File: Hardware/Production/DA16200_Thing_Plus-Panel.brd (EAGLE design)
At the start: 200.2 x 144.3 mm, 2086 parts, among them J1 Qwiic, J10 CORTEX_JTAG_DEBUG_PTH_NS, J11 Qwiic, J13 USB C, J14 THING_PLUS, J15 CORTEX_JTAG_DEBUG_PTH_NS, J16 Qwiic, J18 USB C, J19 THING_PLUS, J2 THING_PLUS, J20 CORTEX_JTAG_DEBUG_PTH_NS, J21 Qwiic, J23 USB C, J24 THING_PLUS, J25 CORTEX_JTAG_DEBUG_PTH_NS, J26 Qwiic, J28 USB C, J29 THING_PLUS, J3 Qwiic, J30 CORTEX_JTAG_DEBUG_PTH_NS, J31 Qwiic, J33 USB C, J34 THING_PLUS, J35 CORTEX_JTAG_DEBUG_PTH_NS, J36 Qwiic, J38 USB C, J39 THING_PLUS, J40 CORTEX_JTAG_DEBUG_PTH_NS, J41 Qwiic, J43 USB C, J44 THING_PLUS, J45 CORTEX_JTAG_DEBUG_PTH_NS, J46 Qwiic, J48 USB C, J49 THING_PLUS, J5 USB C, J50 CORTEX_JTAG_DEBUG_PTH_NS, J51 Qwiic, J53 USB C, J54 THING_PLUS, J55 CORTEX_JTAG_DEBUG_PTH_NS, J56 Qwiic, J58 USB C, J59 THING_PLUS, J60 CORTEX_JTAG_DEBUG_PTH_NS, J61 Qwiic, J63 USB C, J64 THING_PLUS, J65 CORTEX_JTAG_DEBUG_PTH_NS, J66 Qwiic, J68 USB C, J69 THING_PLUS, J7 CORTEX_JTAG_DEBUG_PTH_NS, J70 CORTEX_JTAG_DEBUG_PTH_NS, J71 Qwiic, J73 USB C, J74 THING_PLUS, J75 CORTEX_JTAG_DEBUG_PTH_NS, J76 Qwiic, J78 USB C, J79 THING_PLUS, J8 USB C, J80 CORTEX_JTAG_DEBUG_PTH_NS, J9 THING_PLUS, Q1 20V/4.2A/52mΩ/1.4W, Q10 20V/4.2A/52mΩ/1.4W, Q11 20V/4.2A/52mΩ/1.4W, Q12 20V/4.2A/52mΩ/1.4W, Q13 20V/4.2A/52mΩ/1.4W, Q14 20V/4.2A/52mΩ/1.4W, Q15 20V/4.2A/52mΩ/1.4W, Q16 20V/4.2A/52mΩ/1.4W, Q2 20V/4.2A/52mΩ/1.4W, Q3 20V/4.2A/52mΩ/1.4W, Q4 20V/4.2A/52mΩ/1.4W, Q5 20V/4.2A/52mΩ/1.4W, Q6 20V/4.2A/52mΩ/1.4W, Q7 20V/4.2A/52mΩ/1.4W, Q8 20V/4.2A/52mΩ/1.4W, Q9 20V/4.2A/52mΩ/1.4W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

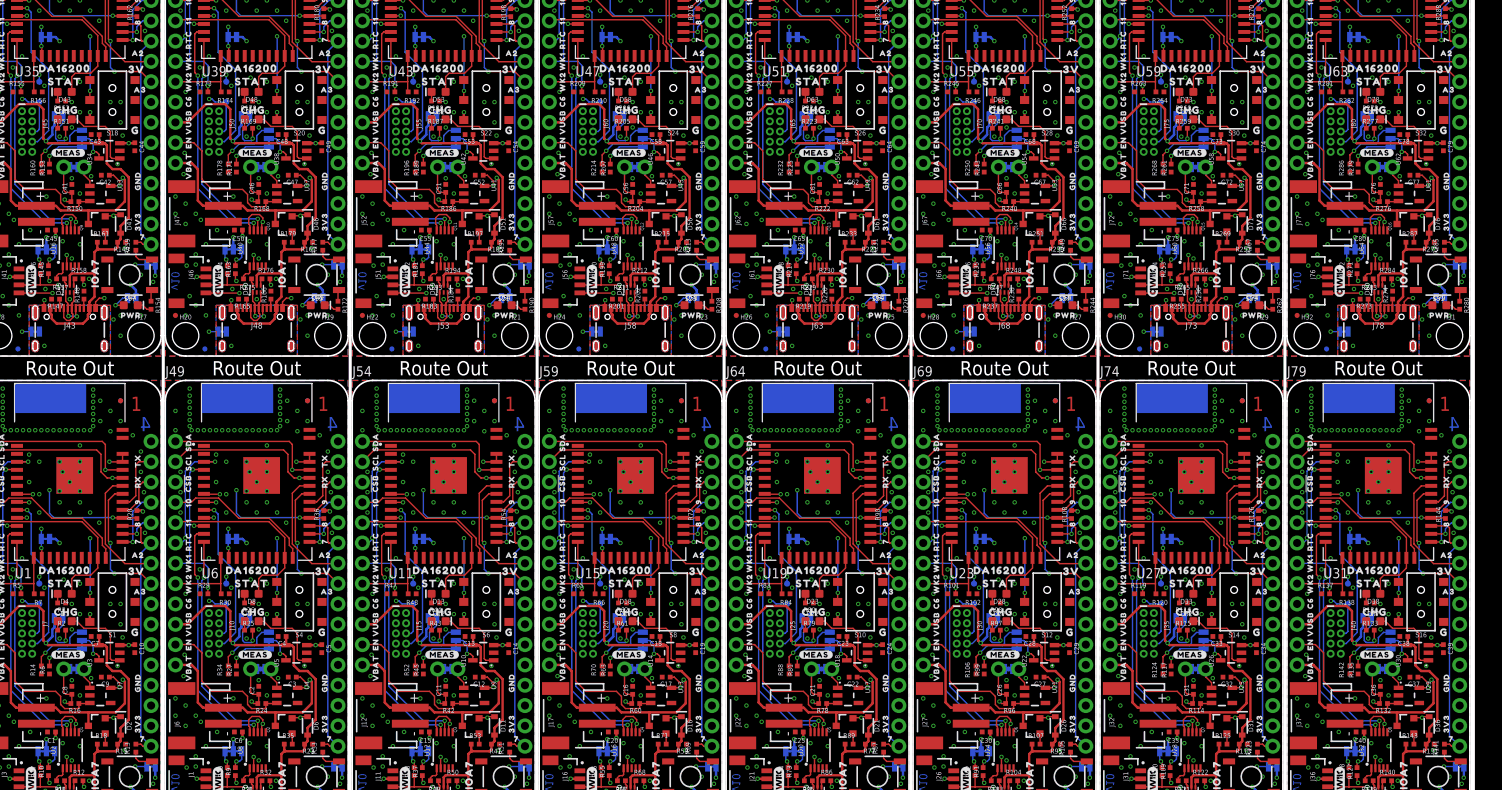
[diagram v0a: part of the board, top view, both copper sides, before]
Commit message: re-panelize
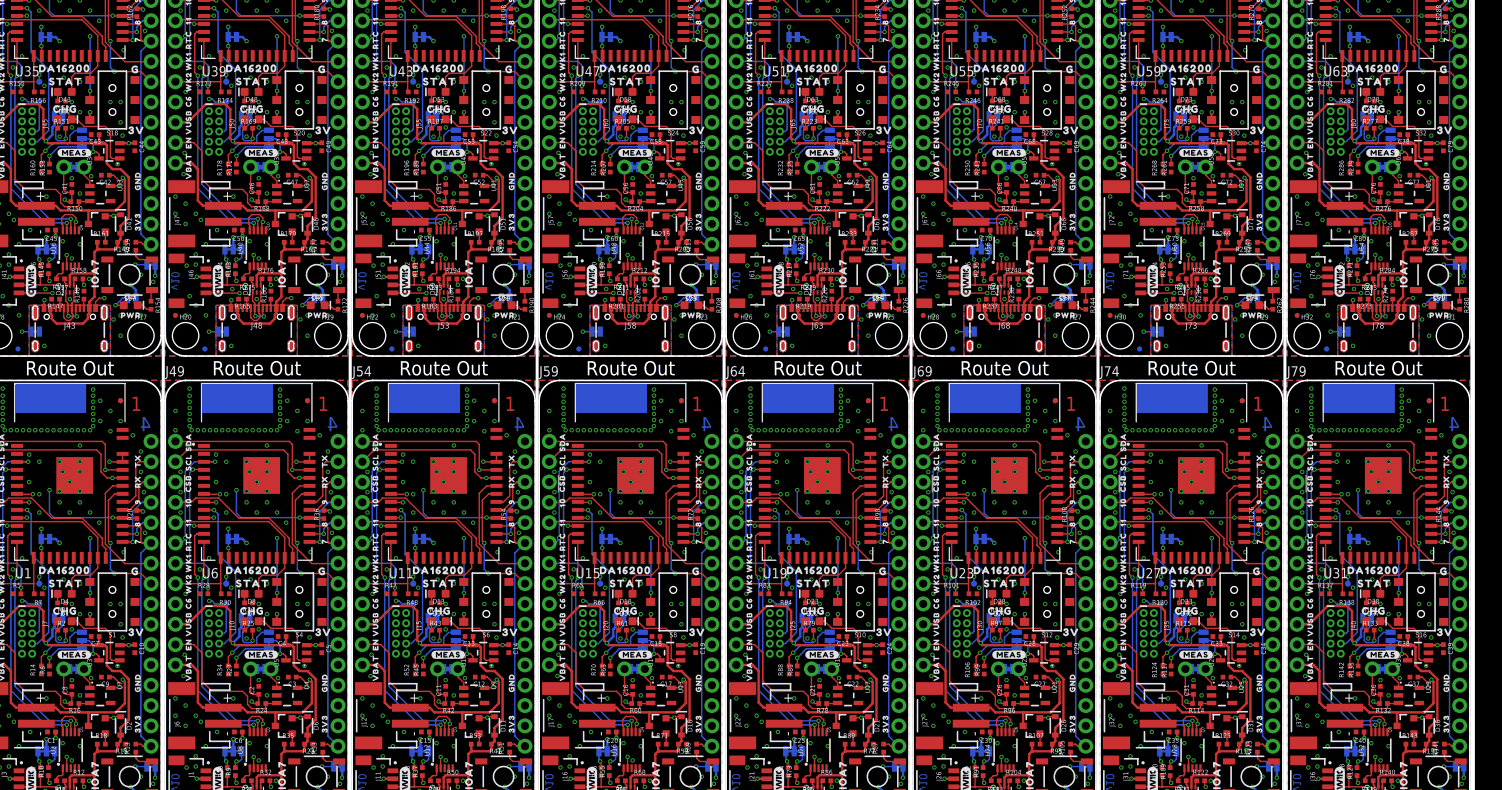
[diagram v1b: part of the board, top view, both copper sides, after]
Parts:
- removed U$1105, U$1106, U$1107, U$1108, U$1109, U$1124: (no value), output:#NC#0
- removed U$1110: (no value), output:5000
- removed U$1111: (no value), output:1000
- removed U$1112: (no value), output:MA0
- removed U$1113: (no value), output:SDA0
- removed U$1114: (no value), output:SCL0
- removed U$1115: (no value), output:#CSB#0
- removed U$1116: (no value), output:100
- removed U$1117: (no value), output:RTC0
- removed U$1118: (no value), output:WK10
- removed U$1119: (no value), output:WK20
- removed U$1120: (no value), output:EN0
- removed U$1121: (no value), output:VUSB0
- removed U$1122: (no value), output:VBAT0
- removed U$1123: (no value), output:110
- removed U$1125: (no value), output:TX0
- removed U$1126: (no value), output:RX0
- removed U$1127: (no value), output:90
- removed U$1128: (no value), output:80
- removed U$1129, U$1134: (no value), output:70
- removed U$1130: (no value), output:A20
- removed U$1131: (no value), output:A30
- removed U$1132: (no value), output:GND0
- removed U$1133: (no value), output:3V30
- removed U$1135: (no value), output:#CHG#0
- removed U$1136: (no value), output:#CH340#0
- removed U$1137: (no value), output:#0#SDA#0
- removed U$1138: (no value), output:#1#SCL#0
- removed U$1139: (no value), output:#6##CSB##0
- removed U$1140: (no value), output:#11#LED#0
- removed U$1141: (no value), output:C60
- removed U$1142: (no value), output:#IOA10#0
- removed U$1143: (no value), output:#4#TXO#0
- removed U$1144: (no value), output:#5#RXI#0
- removed U$1145: (no value), output:#9#POCI#0
- removed U$1146: (no value), output:#8#PICO#0
- removed U$1147: (no value), output:#7#SCLK#0
- removed U$1148: (no value), output:#2#A2#0
- removed U$1149: (no value), output:#3#A3#0
- removed U$1150: (no value), output:#DA#0
- removed U$1151: (no value), output:#MEAS#0
- removed U$1152: (no value), output:#VBAT#0
- U$100, U$169: device output:#NC#0 -> output:1000
- U$1000: device output:#5#RXI#0 -> output:SCL0
- U$1001: device output:#9#POCI#0 -> output:#CSB#0
- U$1002: device output:#8#PICO#0 -> output:100
- U$1003: device output:#7#SCLK#0 -> output:RTC0
- U$1004: device output:#2#A2#0 -> output:WK10
- U$1005: device output:#3#A3#0 -> output:WK20
- U$1006: device output:#DA#0 -> output:EN0
- U$1007: device output:#MEAS#0 -> output:VUSB0
- U$1008: device output:#VBAT#0 -> output:VBAT0
- U$1009: device SparkFun-Aesthetics:QWIIC_4MM -> output:110
- U$101, U$170: device output:#NC#0 -> output:MA0
- U$1010, U$578, U$650: device output:PWR0 -> output:#NC#0
- U$1011: device output:#GND#0 -> output:TX0
- U$1012: device output:#3V3#0 -> output:RX0
- U$1013: device output:#EN#0 -> output:90
- U$1014: device output:#IOC6#0 -> output:80
- U$1015: device output:#WK2#0 -> output:70
- U$1016: device output:#WK1#0 -> output:GND0
- U$1017: device output:#RTC#0 -> output:3V30
- U$1018: device output:THING_PLUS0 -> output:#CHG#0
- U$1019: device output:DA162000 -> output:#CH340#0
- U$102: device output:5000 -> output:SDA0
- U$1020: device output:DA162000 -> output:#0#SDA#0
- U$1021: device output:#I�C#0 -> output:#1#SCL#0
- U$1022: device output:#LED#0 -> output:#6##CSB##0
- U$1023: device output:#SHLD#0 -> output:#11#LED#0
- U$1024: device output:STAT0 -> output:C60
- U$1025: device output:CHG0 -> output:#IOA10#0
- U$1026: device output:##RST##0 -> output:#4#TXO#0
- U$1027: device output:#MEAS#0 -> output:#5#RXI#0
- U$1028: device output:#MEAS_#0 -> output:#9#POCI#0
- U$1029: device output:G0 -> output:#8#PICO#0
- U$103: device output:1000 -> output:SCL0
- U$1030: device output:3V0 -> output:#7#SCLK#0
- U$1031: device output:IOA7_0 -> output:#2#A2#0
- U$1032: device output:#VU#0 -> output:#3#A3#0
- U$1033, U$964: device output:#NC#0 -> output:#DA#0
- U$1034, U$620, U$965: device output:#NC#0 -> output:#MEAS#0
- U$1035: device output:#NC#0 -> output:#VBAT#0
- U$1036: device output:#NC#0 -> SparkFun-Aesthetics:QWIIC_4MM
- U$1037, U$692: device output:#NC#0 -> output:PWR0
- U$1038: device output:5000 -> output:#GND#0
- U$1039: device output:1000 -> output:#3V3#0
- U$104: device output:MA0 -> output:#CSB#0
- U$1040: device output:MA0 -> output:#EN#0
- U$1041: device output:SDA0 -> output:#IOC6#0
- U$1042: device output:SCL0 -> output:#WK2#0
- U$1043: device output:#CSB#0 -> output:#WK1#0
- U$1044: device output:100 -> output:#RTC#0
- U$1045: device output:RTC0 -> output:THING_PLUS0
- U$1046: device output:WK10 -> output:DA162000
- U$1047: device output:WK20 -> output:DA162000
- U$1048: device output:EN0 -> output:#I�C#0
- U$1049: device output:VUSB0 -> output:#LED#0
- U$105: device output:SDA0 -> output:100
- U$1050: device output:VBAT0 -> output:#SHLD#0
- U$1051: device output:110 -> output:STAT0
- U$1052: device output:#NC#0 -> output:CHG0
- U$1053: device output:TX0 -> output:##RST##0
- U$1054: device output:RX0 -> output:#MEAS#0
- U$1055: device output:90 -> output:#MEAS_#0
- U$1056: device output:80 -> output:G0
- U$1057: device output:70 -> output:3V0
- U$1058: device output:A20 -> output:IOA7_0
- U$1059: device output:A30 -> output:#VU#0
- U$106: device output:SCL0 -> output:RTC0
- U$1060: device output:GND0 -> output:#NC#0
- U$1061: device output:3V30 -> output:#NC#0
- U$1062: device output:70 -> output:#NC#0
- U$1063, U$991: device output:#CHG#0 -> output:#NC#0
- U$1064, U$992: device output:#CH340#0 -> output:#NC#0
- U$1065: device output:#0#SDA#0 -> output:5000
- U$1066: device output:#1#SCL#0 -> output:1000
- U$1067: device output:#6##CSB##0 -> output:MA0
- U$1068: device output:#11#LED#0 -> output:SDA0
- U$1069: device output:C60 -> output:SCL0
- U$107: device output:#CSB#0 -> output:WK10
- U$1070: device output:#IOA10#0 -> output:#CSB#0
- U$1071: device output:#4#TXO#0 -> output:100
- U$1072: device output:#5#RXI#0 -> output:RTC0
- U$1073: device output:#9#POCI#0 -> output:WK10
- U$1074: device output:#8#PICO#0 -> output:WK20
- U$1075: device output:#7#SCLK#0 -> output:EN0
- U$1076: device output:#2#A2#0 -> output:VUSB0
- U$1077: device output:#3#A3#0 -> output:VBAT0
- U$1078: device output:#DA#0 -> output:110
- U$1079, U$163, U$235, U$647, U$719: device output:#MEAS#0 -> output:#NC#0
- U$108: device output:100 -> output:WK20
- U$1080: device output:#VBAT#0 -> output:TX0
- U$1081: device SparkFun-Aesthetics:QWIIC_4MM -> output:RX0
- U$1082: device output:PWR0 -> output:90
- U$1083: device output:#GND#0 -> output:80
- U$1084: device output:#3V3#0 -> output:70
- U$1085: device output:#EN#0 -> output:GND0
- U$1086: device output:#IOC6#0 -> output:3V30
- U$1087: device output:#WK2#0 -> output:#CHG#0
- U$1088: device output:#WK1#0 -> output:#CH340#0
- U$1089: device output:#RTC#0 -> output:#0#SDA#0
- U$109: device output:RTC0 -> output:EN0
- U$1090: device output:THING_PLUS0 -> output:#1#SCL#0
- U$1091: device output:DA162000 -> output:#6##CSB##0
- U$1092: device output:DA162000 -> output:#11#LED#0
- U$1093: device output:#I�C#0 -> output:C60
- U$1094: device output:#LED#0 -> output:#IOA10#0
- U$1095: device output:#SHLD#0 -> output:#4#TXO#0
- U$1096: device output:STAT0 -> output:#5#RXI#0
- U$1097: device output:CHG0 -> output:#9#POCI#0
- U$1098: device output:##RST##0 -> output:#8#PICO#0
- U$1099: device output:#MEAS#0 -> output:#7#SCLK#0
- U$110: device output:WK10 -> output:VUSB0
- U$1100: device output:#MEAS_#0 -> output:#2#A2#0
- U$1101: device output:G0 -> output:#3#A3#0
- U$1102: device output:3V0 -> output:#DA#0
- U$1103: device output:IOA7_0 -> output:#MEAS#0
- U$1104: device output:#VU#0 -> output:#VBAT#0
- U$111: device output:WK20 -> output:VBAT0
- U$112: device output:EN0 -> output:110
- U$113: device output:VUSB0 -> output:#NC#0
- U$114: device output:VBAT0 -> output:TX0
- U$115: device output:110 -> output:RX0
- U$116, U$461, U$530: device output:#NC#0 -> output:90
- U$117: device output:TX0 -> output:80
- U$118: device output:RX0 -> output:70
- U$119: device output:90 -> output:GND0
- U$120: device output:80 -> output:3V30
- U$121: device output:70 -> output:#CHG#0
- U$122: device output:A20 -> output:#CH340#0
- U$123: device output:A30 -> output:#0#SDA#0
- U$124: device output:GND0 -> output:#1#SCL#0
- U$125: device output:3V30 -> output:#6##CSB##0
- U$126: device output:70 -> output:#11#LED#0
- U$127: device output:#CHG#0 -> output:C60
- U$128: device output:#CH340#0 -> output:#IOA10#0
- U$129: device output:#0#SDA#0 -> output:#4#TXO#0
- U$130: device output:#1#SCL#0 -> output:#5#RXI#0
- U$131: device output:#6##CSB##0 -> output:#9#POCI#0
- U$132: device output:#11#LED#0 -> output:#8#PICO#0
- U$133: device output:C60 -> output:#7#SCLK#0
- U$134: device output:#IOA10#0 -> output:#2#A2#0
- U$135: device output:#4#TXO#0 -> output:#3#A3#0
- U$136: device output:#5#RXI#0 -> output:#DA#0
- U$137: device output:#9#POCI#0 -> output:#MEAS#0
- U$138: device output:#8#PICO#0 -> output:#VBAT#0
- U$139: device output:#7#SCLK#0 -> SparkFun-Aesthetics:QWIIC_4MM
- U$140: device output:#2#A2#0 -> output:PWR0
- U$141: device output:#3#A3#0 -> output:#GND#0
- U$142: device output:#DA#0 -> output:#3V3#0
- U$143: device output:#MEAS#0 -> output:#EN#0
- U$144: device output:#VBAT#0 -> output:#IOC6#0
- U$145: device SparkFun-Aesthetics:QWIIC_4MM -> output:#WK2#0
- U$146: device output:PWR0 -> output:#WK1#0
- U$147: device output:#GND#0 -> output:#RTC#0
- U$148: device output:#3V3#0 -> output:THING_PLUS0
- U$149: device output:#EN#0 -> output:DA162000
- U$150: device output:#IOC6#0 -> output:DA162000
- U$151: device output:#WK2#0 -> output:#I�C#0
- U$152: device output:#WK1#0 -> output:#LED#0
- U$153: device output:#RTC#0 -> output:#SHLD#0
- U$154: device output:THING_PLUS0 -> output:STAT0
- U$155: device output:DA162000 -> output:CHG0
- U$156: device output:DA162000 -> output:##RST##0
- U$157: device output:#I�C#0 -> output:#MEAS#0
- U$158: device output:#LED#0 -> output:#MEAS_#0
- U$159: device output:#SHLD#0 -> output:G0
- U$160: device output:STAT0 -> output:3V0
- U$161: device output:CHG0 -> output:IOA7_0
- U$162: device output:##RST##0 -> output:#VU#0
- U$164, U$236, U$596: device output:#MEAS_#0 -> output:#NC#0
- U$165: device output:G0 -> output:#NC#0
- U$166, U$94: device output:3V0 -> output:#NC#0
- U$167, U$527, U$95: device output:IOA7_0 -> output:#NC#0
- U$168: device output:#VU#0 -> output:5000
- U$171: device output:#NC#0 -> output:SDA0
- U$172, U$241: device output:#NC#0 -> output:SCL0
- U$173, U$242: device output:#NC#0 -> output:#CSB#0
- U$174: device output:5000 -> output:100
- U$175: device output:1000 -> output:RTC0
- U$176: device output:MA0 -> output:WK10
- U$177: device output:SDA0 -> output:WK20
- U$178: device output:SCL0 -> output:EN0
- U$179: device output:#CSB#0 -> output:VUSB0
- U$180: device output:100 -> output:VBAT0
- U$181: device output:RTC0 -> output:110
- U$182: device output:WK10 -> output:#NC#0
- U$183: device output:WK20 -> output:TX0
- U$184: device output:EN0 -> output:RX0
- U$185: device output:VUSB0 -> output:90
- U$186: device output:VBAT0 -> output:80
- U$187: device output:110 -> output:70
- U$188, U$533, U$602: device output:#NC#0 -> output:GND0
- U$189: device output:TX0 -> output:3V30
- U$190: device output:RX0 -> output:#CHG#0
- U$191: device output:90 -> output:#CH340#0
- U$192: device output:80 -> output:#0#SDA#0
- U$193: device output:70 -> output:#1#SCL#0
- U$194: device output:A20 -> output:#6##CSB##0
- U$195: device output:A30 -> output:#11#LED#0
- U$196: device output:GND0 -> output:C60
- U$197: device output:3V30 -> output:#IOA10#0
- U$198: device output:70 -> output:#4#TXO#0
- U$199: device output:#CHG#0 -> output:#5#RXI#0
- U$200: device output:#CH340#0 -> output:#9#POCI#0
- U$201: device output:#0#SDA#0 -> output:#8#PICO#0
- U$202: device output:#1#SCL#0 -> output:#7#SCLK#0
- U$203: device output:#6##CSB##0 -> output:#2#A2#0
- U$204: device output:#11#LED#0 -> output:#3#A3#0
- U$205: device output:C60 -> output:#DA#0
- U$206: device output:#IOA10#0 -> output:#MEAS#0
- U$207: device output:#4#TXO#0 -> output:#VBAT#0
- U$208: device output:#5#RXI#0 -> SparkFun-Aesthetics:QWIIC_4MM
- U$209: device output:#9#POCI#0 -> output:PWR0
- U$210: device output:#8#PICO#0 -> output:#GND#0
- U$211: device output:#7#SCLK#0 -> output:#3V3#0
- U$212: device output:#2#A2#0 -> output:#EN#0
- U$213: device output:#3#A3#0 -> output:#IOC6#0
- U$214: device output:#DA#0 -> output:#WK2#0
- U$215: device output:#MEAS#0 -> output:#WK1#0
- U$216: device output:#VBAT#0 -> output:#RTC#0
- U$217: device SparkFun-Aesthetics:QWIIC_4MM -> output:THING_PLUS0
- U$218: device output:PWR0 -> output:DA162000
- U$219: device output:#GND#0 -> output:DA162000
- U$220: device output:#3V3#0 -> output:#I�C#0
- U$221: device output:#EN#0 -> output:#LED#0
- U$222: device output:#IOC6#0 -> output:#SHLD#0
- U$223: device output:#WK2#0 -> output:STAT0
- U$224: device output:#WK1#0 -> output:CHG0
- U$225: device output:#RTC#0 -> output:##RST##0
- U$226: device output:THING_PLUS0 -> output:#MEAS#0
- U$227: device output:DA162000 -> output:#MEAS_#0
- U$228: device output:DA162000 -> output:G0
- U$229: device output:#I�C#0 -> output:3V0
- U$230: device output:#LED#0 -> output:IOA7_0
- U$231: device output:#SHLD#0 -> output:#VU#0
- U$232, U$304: device output:STAT0 -> output:#NC#0
- U$233, U$305, U$665: device output:CHG0 -> output:#NC#0
- U$234: device output:##RST##0 -> output:#NC#0
- U$237: device output:G0 -> output:5000
- U$238: device output:3V0 -> output:1000
- U$239: device output:IOA7_0 -> output:MA0
- U$240: device output:#VU#0 -> output:SDA0
- U$243: device output:#NC#0 -> output:100
- U$244, U$313: device output:#NC#0 -> output:RTC0
- U$245, U$314: device output:#NC#0 -> output:WK10
- U$246: device output:5000 -> output:WK20
- U$247: device output:1000 -> output:EN0
- U$248: device output:MA0 -> output:VUSB0
- U$249: device output:SDA0 -> output:VBAT0
- U$250: device output:SCL0 -> output:110
- U$251: device output:#CSB#0 -> output:#NC#0
- U$252: device output:100 -> output:TX0
- U$253: device output:RTC0 -> output:RX0
- U$254: device output:WK10 -> output:90
- U$255: device output:WK20 -> output:80
- U$256: device output:EN0 -> output:70
- U$257: device output:VUSB0 -> output:GND0
- U$258: device output:VBAT0 -> output:3V30
- U$259: device output:110 -> output:#CHG#0
- U$260, U$605, U$674: device output:#NC#0 -> output:#CH340#0
- U$261: device output:TX0 -> output:#0#SDA#0
- U$262: device output:RX0 -> output:#1#SCL#0
- U$263: device output:90 -> output:#6##CSB##0
- U$264: device output:80 -> output:#11#LED#0
- U$265: device output:70 -> output:C60
- U$266: device output:A20 -> output:#IOA10#0
- U$267: device output:A30 -> output:#4#TXO#0
- U$268: device output:GND0 -> output:#5#RXI#0
- U$269: device output:3V30 -> output:#9#POCI#0
- U$270: device output:70 -> output:#8#PICO#0
- U$271: device output:#CHG#0 -> output:#7#SCLK#0
- U$272: device output:#CH340#0 -> output:#2#A2#0
- U$273: device output:#0#SDA#0 -> output:#3#A3#0
- U$274: device output:#1#SCL#0 -> output:#DA#0
- U$275: device output:#6##CSB##0 -> output:#MEAS#0
- U$276: device output:#11#LED#0 -> output:#VBAT#0
- U$277: device output:C60 -> SparkFun-Aesthetics:QWIIC_4MM
- U$278: device output:#IOA10#0 -> output:PWR0
- U$279: device output:#4#TXO#0 -> output:#GND#0
- U$280: device output:#5#RXI#0 -> output:#3V3#0
- U$281: device output:#9#POCI#0 -> output:#EN#0
- U$282: device output:#8#PICO#0 -> output:#IOC6#0
- U$283: device output:#7#SCLK#0 -> output:#WK2#0
- U$284: device output:#2#A2#0 -> output:#WK1#0
- U$285: device output:#3#A3#0 -> output:#RTC#0
- U$286: device output:#DA#0 -> output:THING_PLUS0
- U$287: device output:#MEAS#0 -> output:DA162000
- U$288: device output:#VBAT#0 -> output:DA162000
- U$289: device SparkFun-Aesthetics:QWIIC_4MM -> output:#I�C#0
- U$290: device output:PWR0 -> output:#LED#0
- U$291: device output:#GND#0 -> output:#SHLD#0
- U$292: device output:#3V3#0 -> output:STAT0
- U$293: device output:#EN#0 -> output:CHG0
- U$294: device output:#IOC6#0 -> output:##RST##0
- U$295: device output:#WK2#0 -> output:#MEAS#0
- U$296: device output:#WK1#0 -> output:#MEAS_#0
- U$297: device output:#RTC#0 -> output:G0
- U$298: device output:THING_PLUS0 -> output:3V0
- U$299: device output:DA162000 -> output:IOA7_0
- U$300: device output:DA162000 -> output:#VU#0
- U$301, U$373: device output:#I�C#0 -> output:#NC#0
- U$302, U$374, U$734: device output:#LED#0 -> output:#NC#0
- U$303: device output:#SHLD#0 -> output:#NC#0
- U$306: device output:##RST##0 -> output:5000
- U$307: device output:#MEAS#0 -> output:1000
- U$308: device output:#MEAS_#0 -> output:MA0
- U$309: device output:G0 -> output:SDA0
- U$310: device output:3V0 -> output:SCL0
- U$311: device output:IOA7_0 -> output:#CSB#0
- U$312: device output:#VU#0 -> output:100
- U$315: device output:#NC#0 -> output:WK20
- U$316, U$385: device output:#NC#0 -> output:EN0
- U$317, U$386: device output:#NC#0 -> output:VUSB0
- U$318: device output:5000 -> output:VBAT0
- U$319: device output:1000 -> output:110
- U$320: device output:MA0 -> output:#NC#0
- U$321: device output:SDA0 -> output:TX0
- U$322: device output:SCL0 -> output:RX0
- U$323: device output:#CSB#0 -> output:90
- U$324: device output:100 -> output:80
- U$325: device output:RTC0 -> output:70
- U$326: device output:WK10 -> output:GND0
- U$327: device output:WK20 -> output:3V30
- U$328: device output:EN0 -> output:#CHG#0
- U$329: device output:VUSB0 -> output:#CH340#0
- U$330: device output:VBAT0 -> output:#0#SDA#0
- U$331: device output:110 -> output:#1#SCL#0
- U$332, U$677, U$746: device output:#NC#0 -> output:#6##CSB##0
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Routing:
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
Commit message: Final panel
Kasey generated and approved!
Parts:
- removed C61, C66, C71, C76: 1.0uF, SparkFun-Capacitors:0402-TIGHT
- removed C62, C67, C72, C77: 2.2uF, SparkFun-Capacitors:0402-TIGHT
- removed C63, C64, C68, C69, C73, C74, C78, C79: 4.7uF, SparkFun-Capacitors:0402-TIGHT
- removed C65, C70, C75, C80: 0.1uF, SparkFun-Capacitors:0402-TIGHT
- removed CHG12, CHG13, CHG14, CHG15: JUMPER-SMT_3_1-NC_TRACE_SILK, SparkFun-Jumpers:SMT-JUMPER_3_1-NC_TRACE_SILK
- removed CHG_LED12, CHG_LED13, CHG_LED14, CHG_LED15, CH_PWR12, CH_PWR13, CH_PWR14, CH_PWR15, DA_MEAS12, DA_MEAS13, DA_MEAS14, DA_MEAS15, LED12, LED13, LED14, LED15, SHLD12, SHLD13, SHLD14, SHLD15: JUMPER-SMT_2_NC_TRACE_SILK, SparkFun-Jumpers:SMT-JUMPER_2_NC_TRACE_SILK
- removed D61, D66, D71, D76: 1A/23V/620mV, SparkFun-DiscreteSemi:SOD-323
- removed D62, D67, D72, D77: Yellow, SparkFun-LED:LED-0603
- removed D63, D68, D73, D78: BLUE, SparkFun-LED:LED-0603
- removed D64, D69, D74, D79: RED, SparkFun-LED:LED-0603
- removed D65, D70, D75, D80: PRTR5V0U2F, SparkFun-IC-Power:SOT886
- removed FD49, FD50, FD51, FD52, FD53, FD54, FD55, FD56, FD57, FD58, FD59, FD60, FD61, FD62, FD63, FD64: FIDUCIALUFIDUCIAL, SparkFun-Aesthetics:FIDUCIAL-MICRO
- removed GPIOC13, GPIOC14, GPIOC15, GPIOC16, TMS12, TMS13, TMS14, TMS15: TEST-POINT3, SparkFun-Connectors:PAD.03X.03
- removed H25, H26, H27, H28, H29, H30, H31, H32: STAND-OFF, SparkFun-Hardware:STAND-OFF
- removed I2C_PU12, I2C_PU13, I2C_PU14, I2C_PU15: JUMPER-SMT_3_2-NC_TRACE_SILK, SparkFun-Jumpers:SMT-JUMPER_3_2-NC_TRACE_SILK
- removed J61, J66, J71, J76: Qwiic, SparkFun-Connectors:JST04_1MM_RA
- removed J62, J67, J72, J77: (no value), SparkFun-Connectors:JST-2-SMD
- removed J63, J68, J73, J78: USB C, SparkFun-Connectors:USB-C-16P-4LAYER-ISOLATED
- removed J64, J69, J74, J79: THING_PLUS, SparkFun-Boards:THING_PLUS
- removed J65, J70, J75, J80: CORTEX_JTAG_DEBUG_PTH_NS, SparkFun-Connectors:2X5-PTH-1.27MM-NO_SILK
- removed LOGO25, LOGO27, LOGO29, LOGO31: OSHW-LOGOS, SparkFun-Aesthetics:OSHW-LOGO-S
- removed LOGO26, LOGO28, LOGO30, LOGO32: SFE_LOGO_NAME_FLAME.1_INCH, SparkFun-Aesthetics:SFE_LOGO_NAME_FLAME_.1
- removed MEAS12, MEAS13, MEAS14, MEAS15: JUMPER-COMBO_2_NC_TRACE, SparkFun-Jumpers:COMBO-JUMPER_2_NC_TRACE
- removed Q13, Q14, Q15, Q16: 20V/4.2A/52mΩ/1.4W, SparkFun-DiscreteSemi:SOT23-3
- removed R217, R218, R235, R236, R253, R254, R271, R272: 2.2k, SparkFun-Resistors:0402-TIGHT
- removed R219, R220, R237, R238, R255, R256, R273, R274: 5.1k, SparkFun-Resistors:0402-TIGHT
- removed R221, R222, R232, R234, R239, R240, R250, R252, R257, R258, R268, R270, R275, R276, R286, R288: 10k, SparkFun-Resistors:0402-TIGHT
- removed R223, R224, R226, R241, R242, R244, R259, R260, R262, R277, R278, R280: 1k, SparkFun-Resistors:0402-TIGHT
- removed R225, R243, R261, R279: 2.0K, SparkFun-Resistors:0402-TIGHT
- removed R227, R228, R245, R246, R263, R264, R281, R282: 4.7k, SparkFun-Resistors:0402-TIGHT
- removed R229, R230, R247, R248, R265, R266, R283, R284: 27, SparkFun-Resistors:0402-TIGHT
- removed R231, R249, R267, R285: 200, SparkFun-Resistors:0402-TIGHT
- removed R233, R251, R269, R287: 100, SparkFun-Resistors:0402-TIGHT
- removed S25, S27, S29, S31: MOMENTARY-SWITCH-SPST-SMD-5.2MM-TALL, SparkFun-Switches:TACTILE_SWITCH_SMD_5.2MM
- removed S26, S28, S30, S32: (no value), SparkFun-Switches:SWITCH_DPDT_SMD_AYZ0202
- removed U$1000, U$1069, U$862, U$931: (no value), output:SCL0
- removed U$1001, U$1070, U$863, U$932: (no value), output:#CSB#0
- removed U$1002, U$1071, U$864, U$933: (no value), output:100
- removed U$1003, U$1072, U$865, U$934: (no value), output:RTC0
- removed U$1004, U$1073, U$866, U$935: (no value), output:WK10
- removed U$1005, U$1074, U$867, U$936: (no value), output:WK20
- removed U$1006, U$1075, U$868, U$937: (no value), output:EN0
- removed U$1007, U$1076, U$869, U$938: (no value), output:VUSB0
- removed U$1008, U$1077, U$870, U$939: (no value), output:VBAT0
- removed U$1009, U$1078, U$871, U$940: (no value), output:110
- removed U$1010, U$1060, U$1061, U$1062, U$1063, U$1064, U$1079, U$853, U$854, U$855, U$856, U$857, U$872, U$922, U$923, U$924, U$925, U$926, U$941, U$991, U$992, U$993, U$994, U$995: (no value), output:#NC#0
- removed U$1011, U$1080, U$873, U$942: (no value), output:TX0
- removed U$1012, U$1081, U$874, U$943: (no value), output:RX0
- removed U$1013, U$1082, U$875, U$944: (no value), output:90
- removed U$1014, U$1083, U$876, U$945: (no value), output:80
- removed U$1015, U$1084, U$877, U$946: (no value), output:70
- removed U$1016, U$1085, U$878, U$947: (no value), output:GND0
- removed U$1017, U$1086, U$879, U$948: (no value), output:3V30
- removed U$1018, U$1087, U$880, U$949: (no value), output:#CHG#0
- removed U$1019, U$1088, U$881, U$950: (no value), output:#CH340#0
- removed U$1020, U$1089, U$882, U$951: (no value), output:#0#SDA#0
- removed U$1021, U$1090, U$883, U$952: (no value), output:#1#SCL#0
- removed U$1022, U$1091, U$884, U$953: (no value), output:#6##CSB##0
- removed U$1023, U$1092, U$885, U$954: (no value), output:#11#LED#0
- removed U$1024, U$1093, U$886, U$955: (no value), output:C60
- removed U$1025, U$1094, U$887, U$956: (no value), output:#IOA10#0
- removed U$1026, U$1095, U$888, U$957: (no value), output:#4#TXO#0
- removed U$1027, U$1096, U$889, U$958: (no value), output:#5#RXI#0
- removed U$1028, U$1097, U$890, U$959: (no value), output:#9#POCI#0
- removed U$1029, U$1098, U$891, U$960: (no value), output:#8#PICO#0
- removed U$1030, U$1099, U$892, U$961: (no value), output:#7#SCLK#0
- removed U$1031, U$1100, U$893, U$962: (no value), output:#2#A2#0
- removed U$1032, U$1101, U$894, U$963: (no value), output:#3#A3#0
- removed U$1033, U$1102, U$895, U$964: (no value), output:#DA#0
- removed U$1034, U$1054, U$1103, U$847, U$896, U$916, U$965, U$985: (no value), output:#MEAS#0
- removed U$1035, U$1104, U$897, U$966: (no value), output:#VBAT#0
- removed U$1036, U$829, U$898, U$967: (no value), SparkFun-Aesthetics:QWIIC_4MM
- removed U$1037, U$830, U$899, U$968: (no value), output:PWR0
- removed U$1038, U$831, U$900, U$969: (no value), output:#GND#0
- removed U$1039, U$832, U$901, U$970: (no value), output:#3V3#0
- removed U$1040, U$833, U$902, U$971: (no value), output:#EN#0
- removed U$1041, U$834, U$903, U$972: (no value), output:#IOC6#0
- removed U$1042, U$835, U$904, U$973: (no value), output:#WK2#0
- removed U$1043, U$836, U$905, U$974: (no value), output:#WK1#0
- removed U$1044, U$837, U$906, U$975: (no value), output:#RTC#0
- removed U$1045, U$838, U$907, U$976: (no value), output:THING_PLUS0
- removed U$1046, U$1047, U$839, U$840, U$908, U$909, U$977, U$978: (no value), output:DA162000
- removed U$1048, U$841, U$910, U$979: (no value), output:#I�C#0
- removed U$1049, U$842, U$911, U$980: (no value), output:#LED#0
- removed U$1050, U$843, U$912, U$981: (no value), output:#SHLD#0
- removed U$1051, U$844, U$913, U$982: (no value), output:STAT0
- removed U$1052, U$845, U$914, U$983: (no value), output:CHG0
- removed U$1053, U$846, U$915, U$984: (no value), output:##RST##0
- removed U$1055, U$848, U$917, U$986: (no value), output:#MEAS_#0
- removed U$1056, U$849, U$918, U$987: (no value), output:G0
- removed U$1057, U$850, U$919, U$988: (no value), output:3V0
- removed U$1058, U$851, U$920, U$989: (no value), output:IOA7_0
- removed U$1059, U$852, U$921, U$990: (no value), output:#VU#0
- removed U$1065, U$858, U$927, U$996: (no value), output:5000
- removed U$1066, U$859, U$928, U$997: (no value), output:1000
- removed U$1067, U$860, U$929, U$998: (no value), output:MA0
- removed U$1068, U$861, U$930, U$999: (no value), output:SDA0
- removed U49, U53, U57, U61: XC6222B331MR-G, SparkFun-IC-Power:SOT23-5
- removed U50, U54, U58, U62: MCP73831, SparkFun-IC-Power:SOT23-5
- removed U51, U55, U59, U63: DA16200MOD, SparkFun-RF:XCVR_DA16200MOD-AAC4WA32
- removed U52, U56, U60, U64: CH340E_MSOP10, SparkFun-IC-Comms:MSOP10
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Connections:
- removed net !RESET!/SPI_CLK12: J64.18, J64.28, R231.2, U51.26
- removed net !RESET!/SPI_CLK13: J69.18, J69.28, R249.2, U55.26
- removed net !RESET!/SPI_CLK14: J74.18, J74.28, R267.2, U59.26
- removed net !RESET!/SPI_CLK15: J79.18, J79.28, R285.2, U63.26
- removed net 3.3V12: C62.1, C65.1, CH_PWR12.2, DA_MEAS12.2, I2C_PU12.2, J61.2, J64.27, J65.1, LED12.2, R234.2, S26.1, U49.5
- removed net 3.3V13: C67.1, C70.1, CH_PWR13.2, DA_MEAS13.2, I2C_PU13.2, J66.2, J69.27, J70.1, LED13.2, R252.2, S28.1, U53.5
- removed net 3.3V14: C72.1, C75.1, CH_PWR14.2, DA_MEAS14.2, I2C_PU14.2, J71.2, J74.27, J75.1, LED14.2, R270.2, S30.1, U57.5
- removed net 3.3V15: C77.1, C80.1, CH_PWR15.2, DA_MEAS15.2, I2C_PU15.2, J76.2, J79.27, J80.1, LED15.2, R288.2, S32.1, U61.5
- removed net A_CH25: J64.19, U51.31
- removed net A_CH26: J64.20, U51.30
- removed net A_CH27: J69.19, U55.31
- removed net A_CH28: J69.20, U55.30
- removed net A_CH29: J74.19, U59.31
- removed net A_CH30: J74.20, U59.30
- removed net A_CH31: J79.19, U63.31
- removed net A_CH32: J79.20, U63.30
- removed net EN12: J64.11, R222.1, U49.3
- removed net EN13: J69.11, R240.1, U53.3
- removed net EN14: J74.11, R258.1, U57.3
- removed net EN15: J79.11, R276.1, U61.3
- removed net GND12: C61.2, C62.2, C63.2, C64.2, C65.2, D65.2, J61.1, J62.1, J63.GND, J63.GND2, J64.25, J65.3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
- removed net GND13: C66.2, C67.2, C68.2, C69.2, C70.2, D70.2, J66.1, J67.1, J68.GND, J68.GND2, J69.25, J70.3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
- removed net GND14: C71.2, C72.2, C73.2, C74.2, C75.2, D75.2, J71.1, J72.1, J73.GND, J73.GND2, J74.25, J75.3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
- removed net GND15: C76.2, C77.2, C78.2, C79.2, C80.2, D80.2, J76.1, J77.1, J78.GND, J78.GND2, J79.25, J80.3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
- removed net GPIOA13: J64.4, U51.23
- removed net GPIOA14: J69.4, U55.23
- removed net GPIOA15: J74.4, U59.23
- removed net GPIOA16: J79.4, U63.23
- removed net GPIOC37: J64.9, J65.10, U51.11
- removed net GPIOC38: GPIOC13.1, J65.6, U51.10
- removed net GPIOC39: J65.8, U51.9
- removed net GPIOC40: J69.9, J70.10, U55.11
- removed net GPIOC41: GPIOC14.1, J70.6, U55.10
- removed net GPIOC42: J70.8, U55.9
- removed net GPIOC43: J74.9, J75.10, U59.11
- removed net GPIOC44: GPIOC15.1, J75.6, U59.10
- removed net GPIOC45: J75.8, U59.9
- removed net GPIOC46: J79.9, J80.10, U63.11
- removed net GPIOC47: GPIOC16.1, J80.6, U63.10
- removed net GPIOC48: J80.8, U63.9
- removed net HDR_RTC_WAKE13: J64.8, R228.2, U51.14
- removed net HDR_RTC_WAKE14: J69.8, R246.2, U55.14
- removed net HDR_RTC_WAKE15: J74.8, R264.2, U59.14
- removed net HDR_RTC_WAKE16: J79.8, R282.2, U63.14
- removed net I2C_SCL12: J61.4, J64.2, R217.1, U51.32
- removed net I2C_SCL13: J66.4, J69.2, R235.1, U55.32
- removed net I2C_SCL14: J71.4, J74.2, R253.1, U59.32
- removed net I2C_SCL15: J76.4, J79.2, R271.1, U63.32
- removed net I2C_SDA12: J61.3, J64.1, R218.1, U51.33
- removed net I2C_SDA13: J66.3, J69.1, R236.1, U55.33
- removed net I2C_SDA14: J71.3, J74.1, R254.1, U59.33
- removed net I2C_SDA15: J76.3, J79.1, R272.1, U63.33
- removed net N$325: D62.C, U50.1
- removed net N$326: CHG12.2, U50.5
- removed net N$327: D62.A, R223.1
- removed net N$328: D63.C, R224.2
- removed net N$329: I2C_PU12.3, R217.2
- removed net N$330: I2C_PU12.1, R218.2
- removed net N$331: J63.A5, R219.1
- removed net N$332: J63.B5, R220.1
- removed net N$333: C61.1, D61.C, MEAS12.1, MEAS12.3, Q13.2, R222.2
- removed net N$334: D64.C, R226.2
- removed net N$335: D64.A, LED12.1
- removed net N$336: D65.1, J63.A6, J63.B6
- removed net N$337: D65.3, J63.A7, J63.B7
- removed net N$338: D65.6, R229.1
- removed net N$339: D65.4, R230.1
- removed net N$340: R229.2, U52.1
- removed net N$341: R230.2, U52.2
- removed net N$342: R231.1, S25.3
- removed net N$343: CHG12.3, R225.2
- removed net N$344: CHG12.1, R232.2
- removed net N$345: Q13.1, R233.2
- removed net N$346: J63.SHLD1, J63.SHLD2, J63.SHLD3, J63.SHLD4, J63.SHLD5, J63.SHLD6, J63.SHLD7, J63.SHLD8, SHLD12.2
- removed net N$347: MEAS12.2, MEAS12.4, U49.1
- removed net N$349: CHG_LED12.1, R223.2
- removed net N$350: DA_MEAS12.1, U51.15, U51.34, U51.35
- removed net N$351: CH_PWR12.1, U52.10, U52.7
- removed net N$352: D67.C, U54.1
- removed net N$353: CHG13.2, U54.5
- removed net N$354: D67.A, R241.1
- removed net N$355: D68.C, R242.2
- removed net N$356: I2C_PU13.3, R235.2
- removed net N$357: I2C_PU13.1, R236.2
- removed net N$358: J68.A5, R237.1
- removed net N$359: J68.B5, R238.1
- removed net N$360: C66.1, D66.C, MEAS13.1, MEAS13.3, Q14.2, R240.2
- removed net N$361: D69.C, R244.2
- removed net N$362: D69.A, LED13.1
- removed net N$363: D70.1, J68.A6, J68.B6
- removed net N$364: D70.3, J68.A7, J68.B7
- removed net N$365: D70.6, R247.1
- removed net N$366: D70.4, R248.1
- removed net N$367: R247.2, U56.1
- removed net N$368: R248.2, U56.2
- removed net N$369: R249.1, S27.3
- removed net N$370: CHG13.3, R243.2
- removed net N$371: CHG13.1, R250.2
- removed net N$372: Q14.1, R251.2
- removed net N$373: J68.SHLD1, J68.SHLD2, J68.SHLD3, J68.SHLD4, J68.SHLD5, J68.SHLD6, J68.SHLD7, J68.SHLD8, SHLD13.2
- removed net N$374: MEAS13.2, MEAS13.4, U53.1
- removed net N$376: CHG_LED13.1, R241.2
- removed net N$377: DA_MEAS13.1, U55.15, U55.34, U55.35
- removed net N$378: CH_PWR13.1, U56.10, U56.7
- removed net N$379: D72.C, U58.1
- removed net N$380: CHG14.2, U58.5
- removed net N$381: D72.A, R259.1
- removed net N$382: D73.C, R260.2
- removed net N$383: I2C_PU14.3, R253.2
- removed net N$384: I2C_PU14.1, R254.2
- removed net N$385: J73.A5, R255.1
- removed net N$386: J73.B5, R256.1
- removed net N$387: C71.1, D71.C, MEAS14.1, MEAS14.3, Q15.2, R258.2
- removed net N$388: D74.C, R262.2
- removed net N$389: D74.A, LED14.1
- removed net N$390: D75.1, J73.A6, J73.B6
- removed net N$391: D75.3, J73.A7, J73.B7
- removed net N$392: D75.6, R265.1
- removed net N$393: D75.4, R266.1
- removed net N$394: R265.2, U60.1
- removed net N$395: R266.2, U60.2
- removed net N$396: R267.1, S29.3
- removed net N$397: CHG14.3, R261.2
- removed net N$398: CHG14.1, R268.2
- removed net N$399: Q15.1, R269.2
- removed net N$400: J73.SHLD1, J73.SHLD2, J73.SHLD3, J73.SHLD4, J73.SHLD5, J73.SHLD6, J73.SHLD7, J73.SHLD8, SHLD14.2
- removed net N$401: MEAS14.2, MEAS14.4, U57.1
- removed net N$403: CHG_LED14.1, R259.2
- removed net N$404: DA_MEAS14.1, U59.15, U59.34, U59.35
- removed net N$405: CH_PWR14.1, U60.10, U60.7
- removed net N$406: D77.C, U62.1
- removed net N$407: CHG15.2, U62.5
- removed net N$408: D77.A, R277.1
- removed net N$409: D78.C, R278.2
- removed net N$410: I2C_PU15.3, R271.2
- removed net N$411: I2C_PU15.1, R272.2
- removed net N$412: J78.A5, R273.1
- removed net N$413: J78.B5, R274.1
- removed net N$414: C76.1, D76.C, MEAS15.1, MEAS15.3, Q16.2, R276.2
- removed net N$415: D79.C, R280.2
- removed net N$416: D79.A, LED15.1
- removed net N$417: D80.1, J78.A6, J78.B6
- removed net N$418: D80.3, J78.A7, J78.B7
- removed net N$419: D80.6, R283.1
- removed net N$420: D80.4, R284.1
- removed net N$421: R283.2, U64.1
- removed net N$422: R284.2, U64.2
- removed net N$423: R285.1, S31.3
- removed net N$424: CHG15.3, R279.2
- removed net N$425: CHG15.1, R286.2
- removed net N$426: Q16.1, R287.2
- removed net N$427: J78.SHLD1, J78.SHLD2, J78.SHLD3, J78.SHLD4, J78.SHLD5, J78.SHLD6, J78.SHLD7, J78.SHLD8, SHLD15.2
- removed net N$428: MEAS15.2, MEAS15.4, U61.1
- removed net N$430: CHG_LED15.1, R277.2
- removed net N$431: DA_MEAS15.1, U63.15, U63.34, U63.35
- removed net N$432: CH_PWR15.1, U64.10, U64.7
- removed net RTC_PWR_KEY12: J64.6, S26.2, U51.3
- removed net RTC_PWR_KEY13: J69.6, S28.2, U55.3
- removed net RTC_PWR_KEY14: J74.6, S30.2, U59.3
- removed net RTC_PWR_KEY15: J79.6, S32.2, U63.3
- removed net RTC_WAKE13: J64.7, R227.2, U51.4
- removed net RTC_WAKE14: J69.7, R245.2, U55.4
- removed net RTC_WAKE15: J74.7, R263.2, U59.4
- removed net RTC_WAKE16: J79.7, R281.2, U63.4
- removed net SPI_CSB12: J64.3, R234.1, U51.27
- removed net SPI_CSB13: J69.3, R252.1, U55.27
- removed net SPI_CSB14: J74.3, R270.1, U59.27
- removed net SPI_CSB15: J79.3, R288.1, U63.27
- removed net SPI_PICO12: J64.17, U51.25
- removed net SPI_PICO13: J69.17, U55.25
- removed net SPI_PICO14: J74.17, U59.25
- removed net SPI_PICO15: J79.17, U63.25
- removed net SPI_POCI12: J64.16, U51.24
- removed net SPI_POCI13: J69.16, U55.24
- removed net SPI_POCI14: J74.16, U59.24
- removed net SPI_POCI15: J79.16, U63.24
- removed net STAT_LED12: D63.A, J64.5, U51.22
- removed net STAT_LED13: D68.A, J69.5, U55.22
- removed net STAT_LED14: D73.A, J74.5, U59.22
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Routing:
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- removed copper zone on layer 15, net 3.3V12
- removed copper zone on layer 15, net 3.3V13
- removed copper zone on layer 15, net 3.3V14
- removed copper zone on layer 15, net 3.3V15
- removed copper zone on layer 1, net GND12
- removed copper zone on layer 16, net GND12
- removed copper zone on layer 2, net GND12
- removed copper zone on layer 1, net GND13
- removed copper zone on layer 16, net GND13
- removed copper zone on layer 2, net GND13
- removed copper zone on layer 1, net GND14
- removed copper zone on layer 16, net GND14
- removed copper zone on layer 2, net GND14
- removed copper zone on layer 1, net GND15
- removed copper zone on layer 16, net GND15
- removed copper zone on layer 2, net GND15
- removed copper zone on layer 1, net N$346
- removed copper zone on layer 16, net N$346
- removed copper zone on layer 1, net N$373
- removed copper zone on layer 16, net N$373
- removed copper zone on layer 1, net N$400
- removed copper zone on layer 16, net N$400
- removed copper zone on layer 1, net N$427
- removed copper zone on layer 16, net N$427
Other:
- board size 200.2 x 144.3 mm -> 112.3 x 207 mm
